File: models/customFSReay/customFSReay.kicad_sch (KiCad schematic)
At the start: 8 parts

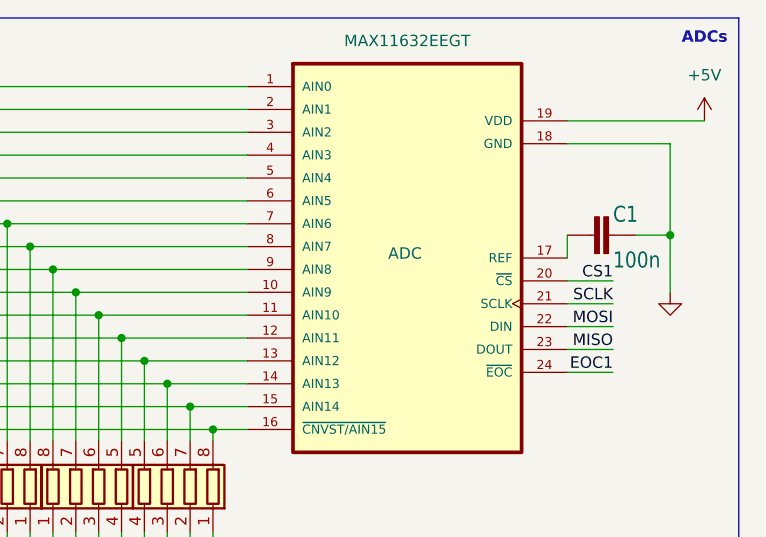
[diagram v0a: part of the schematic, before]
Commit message: modify the fixation position to fit better on finger
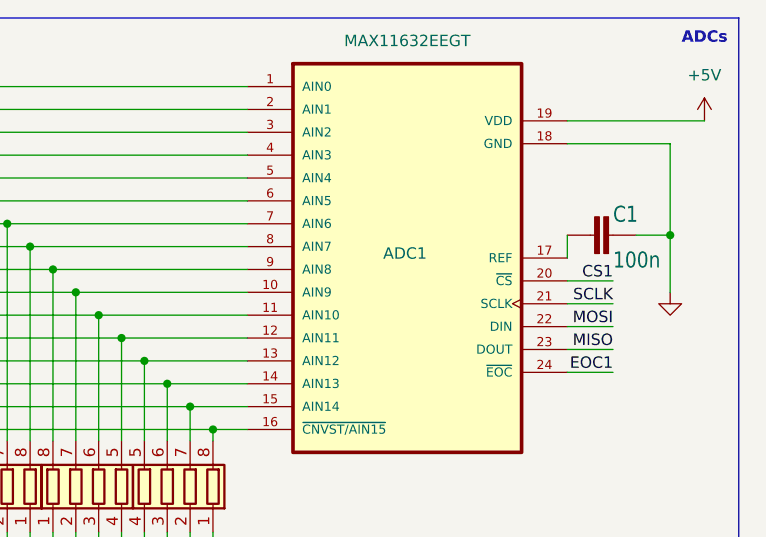
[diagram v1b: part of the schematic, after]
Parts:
- renumbered ADC to ADC1
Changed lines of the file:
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@@
 		(on_board yes)
 		(dnp no)
-		(property "Reference" "ADC"
+		(property "Reference" "ADC1"
 			(at 185.166 61.722 0)
 			(effects
@@
 			(project "customFSReay"
 				(path "/93a34308-6919-422a-bde6-bf7a7695593c"
-					(reference "ADC")
+					(reference "ADC1")
 					(unit 1)
 				)
